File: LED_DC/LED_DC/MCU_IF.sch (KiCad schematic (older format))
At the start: 1 part

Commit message: Removed redundant files
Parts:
- removed J?: Aardvark Header SPI, symbol Connector_Generic:Conn_02x05_Odd_Even
- added J2: Display Port GPIO, symbol Connector_Generic:Conn_02x05_Odd_Even
- added J3: Conn_01x05, symbol Connector_Generic:Conn_01x05
- added R1, R2: 0 R DNP, symbol Device:R
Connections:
- net labels added: I1, I2, I3, I_A, I_B, I_C, I_D, I_DP, I_E, I_F, I_G
- net labels removed: MISO, MOSI, SCLK, SS
- wire segments 10 -> 7
- no-connect marks 2 -> 0
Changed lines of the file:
@@
 $EndDescr
 $Comp
-L Connector_Generic:Conn_02x05_Odd_Even J?
-U 1 1 5FAE5465
-P 2150 2150
-F 0 "J?" H 2200 2567 50  0000 C CNN
-F 1 "Aardvark Header SPI" H 2200 2476 50  0000 C CNN
-F 2 "" H 2150 2150 50  0001 C CNN
-F 3 "~" H 2150 2150 50  0001 C CNN
-	1    2150 2150
+L Connector_Generic:Conn_02x05_Odd_Even J2
+U 1 1 5FB947BB
+P 2200 4650
+F 0 "J2" H 2250 5067 50  0000 C CNN
+F 1 "Display Port GPIO" H 2250 4976 50  0000 C CNN
+F 2 "" H 2200 4650 50  0001 C CNN
+F 3 "~" H 2200 4650 50  0001 C CNN
+	1    2200 4650
 	1    0    0    -1
 $EndComp
-Text GLabel 1950 2250 0    50   BiDi ~ 10
-SCLK
-Text GLabel 1950 2150 0    50   BiDi ~ 10
-MISO
-NoConn ~ 1950 1950
-NoConn ~ 1950 2050
-Text GLabel 1500 2850 0    50   BiDi ~ 10
-SS
-Wire Wire Line
-	1950 2850 1950 2350
-Wire Notes Line
-	1150 3500 1150 1700
 $Comp
-L power:GND #PWR?
-U 1 1 5FAE5F81
-P 3800 2400
-F 0 "#PWR?" H 3800 2150 50  0001 C CNN
-F 1 "GND" H 3805 2227 50  0000 C CNN
-F 2 "" H 3800 2400 50  0001 C CNN
-F 3 "" H 3800 2400 50  0001 C CNN
-	1    3800 2400
+L Connector_Generic:Conn_01x05 J3
+U 1 1 5FB95AE3
+P 4300 4600
+F 0 "J3" H 4380 4642 50  0000 L CNN
+F 1 "Conn_01x05" H 4380 4551 50  0000 L CNN
+F 2 "" H 4300 4600 50  0001 C CNN
+F 3 "~" H 4300 4600 50  0001 C CNN
+	1    4300 4600
 	1    0    0    -1
 $EndComp
-Text GLabel 2450 2250 2    50   BiDi ~ 10
-MOSI
+Text GLabel 2000 4450 0    50   Input ~ 0
+I_A
+Text GLabel 2000 4550 0    50   Input ~ 0
+I_B
+Text GLabel 2000 4650 0    50   Input ~ 0
+I_C
+Text GLabel 2000 4750 0    50   Input ~ 0
+I_D
+Text GLabel 2000 4850 0    50   Input ~ 0
+I_E
+Text GLabel 2500 4450 2    50   Input ~ 0
+I_F
+Text GLabel 2500 4550 2    50   Input ~ 0
+I_G
+Text GLabel 2500 4650 2    50   Input ~ 0
+I1
+Text GLabel 2500 4750 2    50   Input ~ 0
+I2
+Text GLabel 2500 4850 2    50   Input ~ 0
+I3
+$Comp
+L power:+3.3V #PWR05
+U 1 1 5FB981B2
+P 4100 4400
+F 0 "#PWR05" H 4100 4250 50  0001 C CNN
+F 1 "+3.3V" V 4115 4528 50  0000 L CNN
+F 2 "" H 4100 4400 50  0001 C CNN
+F 3 "" H 4100 4400 50  0001 C CNN
+	1    4100 4400
+	0    -1   -1   0
+$EndComp
+$Comp
+L power:GND #PWR03
+U 1 1 5FB98766
+P 3600 4500
+F 0 "#PWR03" H 3600 4250 50  0001 C CNN
+F 1 "GND" H 3605 4327 50  0000 C CNN
+F 2 "" H 3600 4500 50  0001 C CNN
+F 3 "" H 3600 4500 50  0001 C CNN
+	1    3600 4500
+	1    0    0    -1
+$EndComp
 Wire Wire Line
-	3800 1950 3800 2350
-Connection ~ 3800 2350
-Wire Wire Line
-	3800 2350 3800 2400
-Wire Wire Line
-	2450 2350 3300 2350
-Wire Wire Line
-	2450 1950 3800 1950
+	3600 4500 4100 4500
 $Comp
-L power:+3.3V #PWR?
-U 1 1 5FBC99A7
-P 3150 2050
-F 0 "#PWR?" H 3150 1900 50  0001 C CNN
-F 1 "+3.3V" V 3165 2178 50  0000 L CNN
-F 2 "" H 3150 2050 50  0001 C CNN
-F 3 "" H 3150 2050 50  0001 C CNN
-	1    3150 2050
+L power:+5V #PWR06
+U 1 1 5FB9901F
+P 4100 4800
+F 0 "#PWR06" H 4100 4650 50  0001 C CNN
+F 1 "+5V" V 4115 4928 50  0000 L CNN
+F 2 "" H 4100 4800 50  0001 C CNN
+F 3 "" H 4100 4800 50  0001 C CNN
+	1    4100 4800
+	0    -1   -1   0
+$EndComp
+Text GLabel 3150 5200 0    50   Input ~ 0
+I_DP
+Wire Notes Line
+	5450 4000 5450 5950
+Wire Notes Line
+	5450 5950 1150 5950
+Wire Notes Line
+	1150 5950 1150 4000
+Wire Notes Line
+	1150 4000 5450 4000
+Text GLabel 3150 4800 0    50   Input ~ 0
+I_DP
+$Comp
+L Device:R R1
+U 1 1 5FBA047F
+P 3300 4800
+F 0 "R1" V 3093 4800 50  0000 C CNN
+F 1 "0 R DNP" V 3184 4800 50  0000 C CNN
+F 2 "" V 3230 4800 50  0001 C CNN
+F 3 "~" H 3300 4800 50  0001 C CNN
+	1    3300 4800
 	0    1    1    0
 $EndComp
 $Comp
-L power:+5V #PWR?
-U 1 1 5FBD0134
-P 3450 2150
-F 0 "#PWR?" H 3450 2000 50  0001 C CNN
-F 1 "+5V" V 3465 2278 50  0000 L CNN
-F 2 "" H 3450 2150 50  0001 C CNN
-F 3 "" H 3450 2150 50  0001 C CNN
-	1    3450 2150
+L Device:R R2
+U 1 1 5FBA0B04
+P 3300 5200
+F 0 "R2" V 3093 5200 50  0000 C CNN
+F 1 "0 R DNP" V 3184 5200 50  0000 C CNN
+F 2 "" V 3230 5200 50  0001 C CNN
+F 3 "~" H 3300 5200 50  0001 C CNN
+	1    3300 5200
 	0    1    1    0
 $EndComp
-Wire Notes Line
-	4050 1700 4050 3500
-Wire Notes Line
-	1150 3500 4050 3500
-Wire Notes Line
-	1150 1700 4050 1700
 Wire Wire Line
-	1500 2850 1950 2850
+	3450 4800 3700 4800
 Wire Wire Line
-	2450 2050 3150 2050
+	3700 4800 3700 4600
 Wire Wire Line
-	2450 2150 3450 2150
-$Comp
-L power:PWR_FLAG #FLG?
-U 1 1 5FC351CF
-P 3300 2700
-F 0 "#FLG?" H 3300 2775 50  0001 C CNN
-F 1 "PWR_FLAG" H 3300 2873 50  0000 C CNN
-F 2 "" H 3300 2700 50  0001 C CNN
-F 3 "~" H 3300 2700 50  0001 C CNN
-	1    3300 2700
-	-1   0    0    1
-$EndComp
+	3700 4600 4100 4600
 Wire Wire Line
-	3300 2700 3300 2350
-Connection ~ 3300 2350
+	3450 5200 3750 5200
 Wire Wire Line
-	3300 2350 3800 2350
+	3750 5200 3750 4700
+Wire Wire Line
+	3750 4700 4100 4700
 $EndSCHEMATC

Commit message: updated the led schematic.
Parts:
- removed R1, R2: 0 R DNP, symbol Device:R
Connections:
- net labels added: C1, C2, C3, D0, D1, D2, D3, D4, D5, D6, D7
- net labels removed: +3.3V, I1, I2, I3, I_A, I_B, I_C, I_D, I_DP, I_E, I_F, I_G
- wire segments 7 -> 10
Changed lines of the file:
@@
 	1    0    0    -1
 $EndComp
-Text GLabel 2000 4450 0    50   Input ~ 0
-I_A
-Text GLabel 2000 4550 0    50   Input ~ 0
-I_B
-Text GLabel 2000 4650 0    50   Input ~ 0
-I_C
-Text GLabel 2000 4750 0    50   Input ~ 0
-I_D
-Text GLabel 2000 4850 0    50   Input ~ 0
-I_E
-Text GLabel 2500 4450 2    50   Input ~ 0
-I_F
-Text GLabel 2500 4550 2    50   Input ~ 0
-I_G
-Text GLabel 2500 4650 2    50   Input ~ 0
-I1
-Text GLabel 2500 4750 2    50   Input ~ 0
-I2
-Text GLabel 2500 4850 2    50   Input ~ 0
-I3
-$Comp
-L power:+3.3V #PWR05
-U 1 1 5FB981B2
-P 4100 4400
-F 0 "#PWR05" H 4100 4250 50  0001 C CNN
-F 1 "+3.3V" V 4115 4528 50  0000 L CNN
-F 2 "" H 4100 4400 50  0001 C CNN
-F 3 "" H 4100 4400 50  0001 C CNN
-	1    4100 4400
-	0    -1   -1   0
-$EndComp
+Text GLabel 2000 4550 0    50   Output ~ 0
+D1
+Text GLabel 2000 4650 0    50   Output ~ 0
+D3
+Text GLabel 2000 4750 0    50   Output ~ 0
+D5
+Text GLabel 2000 4850 0    50   Output ~ 0
+D7
+Text GLabel 2500 4450 2    50   Output ~ 0
+D0
+Text GLabel 2500 4550 2    50   Output ~ 0
+D2
+Text GLabel 2500 4650 2    50   Output ~ 0
+D4
+Text GLabel 2500 4750 2    50   Output ~ 0
+D6
 $Comp
 L power:GND #PWR03
 U 1 1 5FB98766
-P 3600 4500
-F 0 "#PWR03" H 3600 4250 50  0001 C CNN
-F 1 "GND" H 3605 4327 50  0000 C CNN
-F 2 "" H 3600 4500 50  0001 C CNN
-F 3 "" H 3600 4500 50  0001 C CNN
-	1    3600 4500
+P 4000 4850
+F 0 "#PWR03" H 4000 4600 50  0001 C CNN
+F 1 "GND" H 4005 4677 50  0000 C CNN
+F 2 "" H 4000 4850 50  0001 C CNN
+F 3 "" H 4000 4850 50  0001 C CNN
+	1    4000 4850
 	1    0    0    -1
 $EndComp
-Wire Wire Line
-	3600 4500 4100 4500
 $Comp
 L power:+5V #PWR06
 U 1 1 5FB9901F
-P 4100 4800
-F 0 "#PWR06" H 4100 4650 50  0001 C CNN
-F 1 "+5V" V 4115 4928 50  0000 L CNN
-F 2 "" H 4100 4800 50  0001 C CNN
-F 3 "" H 4100 4800 50  0001 C CNN
-	1    4100 4800
+P 4000 4400
+F 0 "#PWR06" H 4000 4250 50  0001 C CNN
+F 1 "+5V" V 4015 4528 50  0000 L CNN
+F 2 "" H 4000 4400 50  0001 C CNN
+F 3 "" H 4000 4400 50  0001 C CNN
+	1    4000 4400
 	0    -1   -1   0
 $EndComp
-Text GLabel 3150 5200 0    50   Input ~ 0
-I_DP
+Text GLabel 4000 4600 0    50   Output ~ 0
+C2
 Wire Notes Line
 	5450 4000 5450 5950
@@
 Wire Notes Line
 	1150 4000 5450 4000
-Text GLabel 3150 4800 0    50   Input ~ 0
-I_DP
+Text GLabel 4000 4500 0    50   Output ~ 0
+C1
 $Comp
-L Device:R R1
-U 1 1 5FBA047F
-P 3300 4800
-F 0 "R1" V 3093 4800 50  0000 C CNN
-F 1 "0 R DNP" V 3184 4800 50  0000 C CNN
-F 2 "" V 3230 4800 50  0001 C CNN
-F 3 "~" H 3300 4800 50  0001 C CNN
-	1    3300 4800
-	0    1    1    0
+L power:+5V #PWR?
+U 1 1 5FD76D33
+P 1850 4400
+F 0 "#PWR?" H 1850 4250 50  0001 C CNN
+F 1 "+5V" H 1865 4573 50  0000 C CNN
+F 2 "" H 1850 4400 50  0001 C CNN
+F 3 "" H 1850 4400 50  0001 C CNN
+	1    1850 4400
+	1    0    0    -1
 $EndComp
 $Comp
-L Device:R R2
-U 1 1 5FBA0B04
-P 3300 5200
-F 0 "R2" V 3093 5200 50  0000 C CNN
-F 1 "0 R DNP" V 3184 5200 50  0000 C CNN
-F 2 "" V 3230 5200 50  0001 C CNN
-F 3 "~" H 3300 5200 50  0001 C CNN
-	1    3300 5200
-	0    1    1    0
+L power:GND #PWR?
+U 1 1 5FD77C16
+P 2600 4950
+F 0 "#PWR?" H 2600 4700 50  0001 C CNN
+F 1 "GND" H 2605 4777 50  0000 C CNN
+F 2 "" H 2600 4950 50  0001 C CNN
+F 3 "" H 2600 4950 50  0001 C CNN
+	1    2600 4950
+	1    0    0    -1
 $EndComp
 Wire Wire Line
-	3450 4800 3700 4800
+	2600 4950 2600 4850
 Wire Wire Line
-	3700 4800 3700 4600
+	2600 4850 2500 4850
 Wire Wire Line
-	3700 4600 4100 4600
+	1850 4400 1850 4450
 Wire Wire Line
-	3450 5200 3750 5200
+	1850 4450 2000 4450
 Wire Wire Line
-	3750 5200 3750 4700
+	4000 4400 4100 4400
 Wire Wire Line
-	3750 4700 4100 4700
+	4100 4800 4000 4800
+Wire Wire Line
+	4000 4800 4000 4850
+Text GLabel 4000 4700 0    50   Output ~ 0
+C3
+Wire Wire Line
+	4000 4500 4100 4500
+Wire Wire Line
+	4100 4600 4000 4600
+Wire Wire Line
+	4000 4700 4100 4700
 $EndSCHEMATC

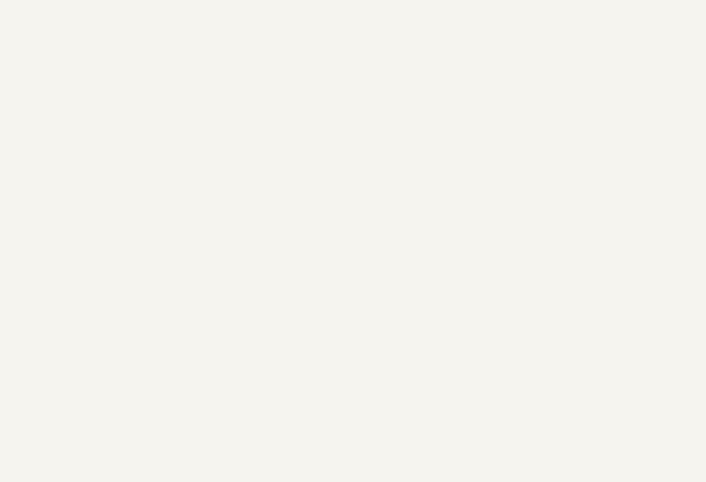
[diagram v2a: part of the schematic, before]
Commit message: Added keypad connector.
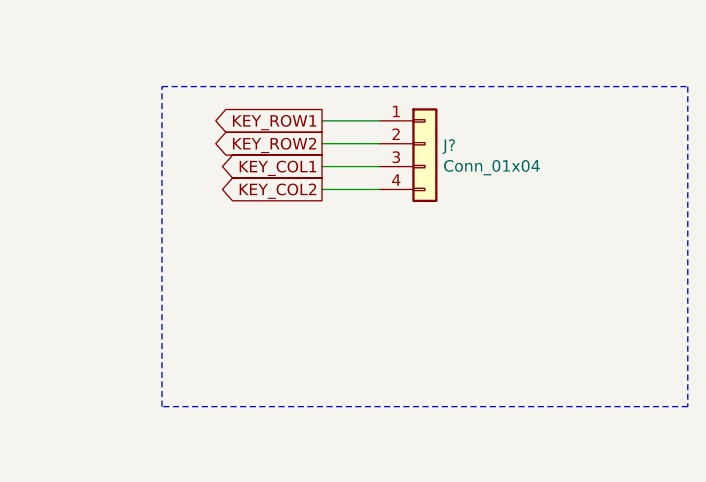
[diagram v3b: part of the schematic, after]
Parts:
- added J?: Conn_01x04, symbol Connector_Generic:Conn_01x04
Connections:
- new net KEY_COL1: J?.3 (Pin_3)
- new net KEY_COL2: J?.4 (Pin_4)
- new net KEY_ROW1: J?.1 (Pin_1)
- new net KEY_ROW2: J?.2 (Pin_2)
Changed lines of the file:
@@
 $Descr A4 11693 8268
 encoding utf-8
-Sheet 2 4
+Sheet 2 5
 Title ""
 Date ""
@@
 Wire Wire Line
 	4000 4700 4100 4700
+$Comp
+L Connector_Generic:Conn_01x04 J?
+U 1 1 5FEC60A3
+P 7400 4550
+F 0 "J?" H 7480 4542 50  0000 L CNN
+F 1 "Conn_01x04" H 7480 4451 50  0000 L CNN
+F 2 "" H 7400 4550 50  0001 C CNN
+F 3 "~" H 7400 4550 50  0001 C CNN
+	1    7400 4550
+	1    0    0    -1
+$EndComp
+Text GLabel 6950 4450 0    50   Output ~ 0
+KEY_ROW1
+Text GLabel 6950 4550 0    50   Output ~ 0
+KEY_ROW2
+Text GLabel 6950 4650 0    50   Output ~ 0
+KEY_COL1
+Text GLabel 6950 4750 0    50   Output ~ 0
+KEY_COL2
+Wire Wire Line
+	6950 4450 7200 4450
+Wire Wire Line
+	7200 4550 6950 4550
+Wire Wire Line
+	6950 4650 7200 4650
+Wire Wire Line
+	7200 4750 6950 4750
+Wire Notes Line
+	8550 4300 8550 5700
+Wire Notes Line
+	8550 5700 6250 5700
+Wire Notes Line
+	6250 5700 6250 4300
+Wire Notes Line
+	6250 4300 8550 4300
 $EndSCHEMATC

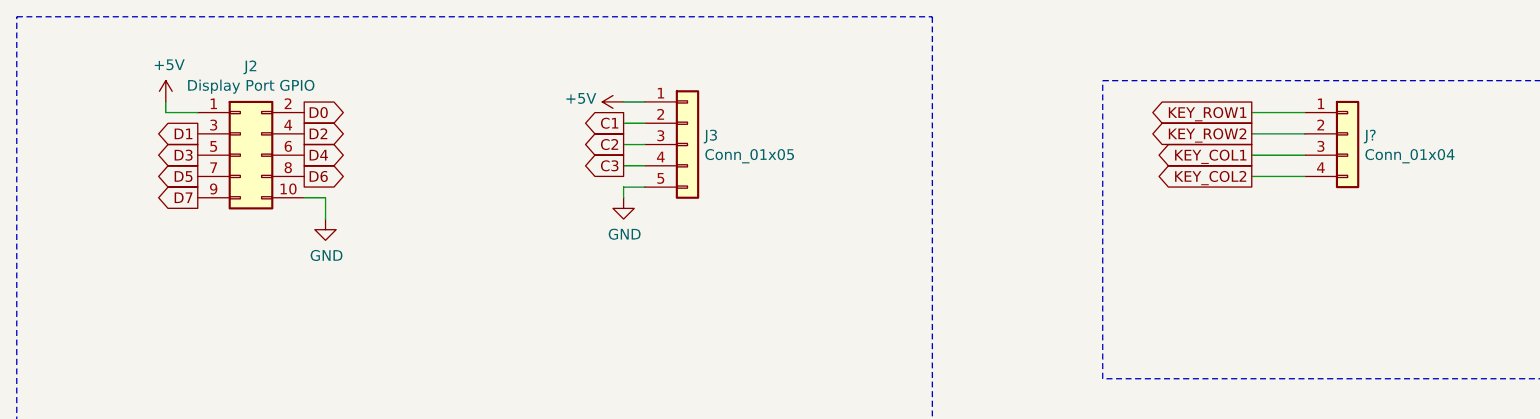
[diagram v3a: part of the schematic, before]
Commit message: Added foot prints for the components.
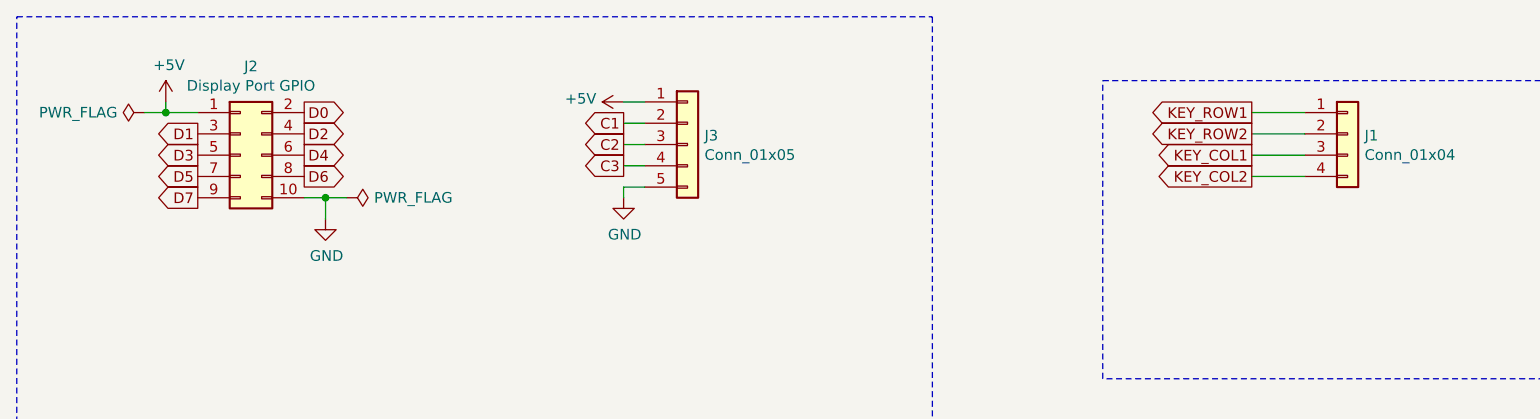
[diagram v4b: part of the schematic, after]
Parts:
- J1: renamed from J?; footprint (none) -> Connector_PinHeader_2.54mm:PinHeader_1x04_P2.54mm_Vertical
- J2: footprint (none) -> Connector_PinHeader_2.54mm:PinHeader_2x05_P2.54mm_Vertical
- J3: footprint (none) -> Connector_PinHeader_2.54mm:PinHeader_1x05_P2.54mm_Vertical
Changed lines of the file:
@@
 F 0 "J2" H 2250 5067 50  0000 C CNN
 F 1 "Display Port GPIO" H 2250 4976 50  0000 C CNN
-F 2 "" H 2200 4650 50  0001 C CNN
+F 2 "Connector_PinHeader_2.54mm:PinHeader_2x05_P2.54mm_Vertical" H 2200 4650 50  0001 C CNN
 F 3 "~" H 2200 4650 50  0001 C CNN
 	1    2200 4650
@@
 F 0 "J3" H 4380 4642 50  0000 L CNN
 F 1 "Conn_01x05" H 4380 4551 50  0000 L CNN
-F 2 "" H 4300 4600 50  0001 C CNN
+F 2 "Connector_PinHeader_2.54mm:PinHeader_1x05_P2.54mm_Vertical" H 4300 4600 50  0001 C CNN
 F 3 "~" H 4300 4600 50  0001 C CNN
 	1    4300 4600
@@
 C1
 $Comp
-L power:+5V #PWR?
+L power:+5V #PWR01
 U 1 1 5FD76D33
 P 1850 4400
-F 0 "#PWR?" H 1850 4250 50  0001 C CNN
+F 0 "#PWR01" H 1850 4250 50  0001 C CNN
 F 1 "+5V" H 1865 4573 50  0000 C CNN
 F 2 "" H 1850 4400 50  0001 C CNN
@@
 $EndComp
 $Comp
-L power:GND #PWR?
+L power:GND #PWR02
 U 1 1 5FD77C16
 P 2600 4950
-F 0 "#PWR?" H 2600 4700 50  0001 C CNN
+F 0 "#PWR02" H 2600 4700 50  0001 C CNN
 F 1 "GND" H 2605 4777 50  0000 C CNN
 F 2 "" H 2600 4950 50  0001 C CNN
@@
 	4000 4700 4100 4700
 $Comp
-L Connector_Generic:Conn_01x04 J?
+L Connector_Generic:Conn_01x04 J1
 U 1 1 5FEC60A3
 P 7400 4550
-F 0 "J?" H 7480 4542 50  0000 L CNN
+F 0 "J1" H 7480 4542 50  0000 L CNN
 F 1 "Conn_01x04" H 7480 4451 50  0000 L CNN
-F 2 "" H 7400 4550 50  0001 C CNN
+F 2 "Connector_PinHeader_2.54mm:PinHeader_1x04_P2.54mm_Vertical" H 7400 4550 50  0001 C CNN
 F 3 "~" H 7400 4550 50  0001 C CNN
 	1    7400 4550
@@
 	7200 4550 6950 4550
 Wire Wire Line
-	6950 4650 7200 4650
-Wire Wire Line
 	7200 4750 6950 4750
 Wire Notes Line
@@
 Wire Notes Line
 	6250 4300 8550 4300
+Wire Wire Line
+	7200 4650 6950 4650
+$Comp
+L power:PWR_FLAG #FLG0101
+U 1 1 5FF0A6FB
+P 1750 4450
+F 0 "#FLG0101" H 1750 4525 50  0001 C CNN
+F 1 "PWR_FLAG" V 1750 4577 50  0000 L CNN
+F 2 "" H 1750 4450 50  0001 C CNN
+F 3 "~" H 1750 4450 50  0001 C CNN
+	1    1750 4450
+	0    -1   -1   0
+$EndComp
+$Comp
+L power:PWR_FLAG #FLG0102
+U 1 1 5FF0AD0F
+P 2700 4850
+F 0 "#FLG0102" H 2700 4925 50  0001 C CNN
+F 1 "PWR_FLAG" V 2700 4978 50  0000 L CNN
+F 2 "" H 2700 4850 50  0001 C CNN
+F 3 "~" H 2700 4850 50  0001 C CNN
+	1    2700 4850
+	0    1    1    0
+$EndComp
+Wire Wire Line
+	2700 4850 2600 4850
+Connection ~ 2600 4850
+Wire Wire Line
+	1750 4450 1850 4450
+Connection ~ 1850 4450
 $EndSCHEMATC

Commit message: updated the foot print assignment.
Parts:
- added H1, H2, H3, H4: MountingHole_Pad, MountingHole:MountingHole_2.2mm_M2_DIN965_Pad, symbol Mechanical:MountingHole_Pad
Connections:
- net GND: now also H1.1, H2.1, H3.1, H4.1
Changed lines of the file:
@@
 	1750 4450 1850 4450
 Connection ~ 1850 4450
+$Comp
+L Mechanical:MountingHole_Pad H1
+U 1 1 5FF5004C
+P 8300 1500
+F 0 "H1" H 8400 1503 50  0000 L CNN
+F 1 "MountingHole_Pad" H 8400 1458 50  0001 L CNN
+F 2 "MountingHole:MountingHole_2.2mm_M2_DIN965_Pad" H 8300 1500 50  0001 C CNN
+F 3 "~" H 8300 1500 50  0001 C CNN
+	1    8300 1500
+	1    0    0    -1
+$EndComp
+$Comp
+L power:GND #PWR023
+U 1 1 5FF505F7
+P 8300 1750
+F 0 "#PWR023" H 8300 1500 50  0001 C CNN
+F 1 "GND" H 8305 1577 50  0000 C CNN
+F 2 "" H 8300 1750 50  0001 C CNN
+F 3 "" H 8300 1750 50  0001 C CNN
+	1    8300 1750
+	1    0    0    -1
+$EndComp
+Wire Wire Line
+	8300 1750 8300 1600
+$Comp
+L Mechanical:MountingHole_Pad H2
+U 1 1 5FF5174B
+P 8700 1500
+F 0 "H2" H 8800 1503 50  0000 L CNN
+F 1 "MountingHole_Pad" H 8800 1458 50  0001 L CNN
+F 2 "MountingHole:MountingHole_2.2mm_M2_DIN965_Pad" H 8700 1500 50  0001 C CNN
+F 3 "~" H 8700 1500 50  0001 C CNN
+	1    8700 1500
+	1    0    0    -1
+$EndComp
+$Comp
+L power:GND #PWR024
+U 1 1 5FF51751
+P 8700 1750
+F 0 "#PWR024" H 8700 1500 50  0001 C CNN
+F 1 "GND" H 8705 1577 50  0000 C CNN
+F 2 "" H 8700 1750 50  0001 C CNN
+F 3 "" H 8700 1750 50  0001 C CNN
+	1    8700 1750
+	1    0    0    -1
+$EndComp
+Wire Wire Line
+	8700 1750 8700 1600
+$Comp
+L Mechanical:MountingHole_Pad H3
+U 1 1 5FF524B0
+P 9100 1500
+F 0 "H3" H 9200 1503 50  0000 L CNN
+F 1 "MountingHole_Pad" H 9200 1458 50  0001 L CNN
+F 2 "MountingHole:MountingHole_2.2mm_M2_DIN965_Pad" H 9100 1500 50  0001 C CNN
+F 3 "~" H 9100 1500 50  0001 C CNN
+	1    9100 1500
+	1    0    0    -1
+$EndComp
+$Comp
+L power:GND #PWR025
+U 1 1 5FF524B6
+P 9100 1750
+F 0 "#PWR025" H 9100 1500 50  0001 C CNN
+F 1 "GND" H 9105 1577 50  0000 C CNN
+F 2 "" H 9100 1750 50  0001 C CNN
+F 3 "" H 9100 1750 50  0001 C CNN
+	1    9100 1750
+	1    0    0    -1
+$EndComp
+Wire Wire Line
+	9100 1750 9100 1600
+$Comp
+L Mechanical:MountingHole_Pad H4
+U 1 1 5FF5377F
+P 9450 1500
+F 0 "H4" H 9550 1503 50  0000 L CNN
+F 1 "MountingHole_Pad" H 9550 1458 50  0001 L CNN
+F 2 "MountingHole:MountingHole_2.2mm_M2_DIN965_Pad" H 9450 1500 50  0001 C CNN
+F 3 "~" H 9450 1500 50  0001 C CNN
+	1    9450 1500
+	1    0    0    -1
+$EndComp
+$Comp
+L power:GND #PWR026
+U 1 1 5FF53785
+P 9450 1750
+F 0 "#PWR026" H 9450 1500 50  0001 C CNN
+F 1 "GND" H 9455 1577 50  0000 C CNN
+F 2 "" H 9450 1750 50  0001 C CNN
+F 3 "" H 9450 1750 50  0001 C CNN
+	1    9450 1750
+	1    0    0    -1
+$EndComp
+Wire Wire Line
+	9450 1750 9450 1600
+Wire Notes Line
+	9800 1300 9800 2100
+Wire Notes Line
+	9800 2100 8050 2100
+Wire Notes Line
+	8050 2100 8050 1300
+Wire Notes Line
+	8050 1300 9800 1300
 $EndSCHEMATC
